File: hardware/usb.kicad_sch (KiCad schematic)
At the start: 35 parts, among them J1 USB_A_Stacked, J2 USB_C_Receptacle_USB2.0_14P, J3 USB_C_Receptacle_USB2.0_14P, J4 USB_C_Receptacle_USB2.0_14P, U10 SY6280AAC, U11 SY6280AAC, U12 SY6280AAC, U13 TPD2EUSB30, U14 TPD2EUSB30, U15 TPD2EUSB30, U16 TPD2EUSB30, U17 HUSB237, U18 TPD2EUSB30, U9 SY6280AAC

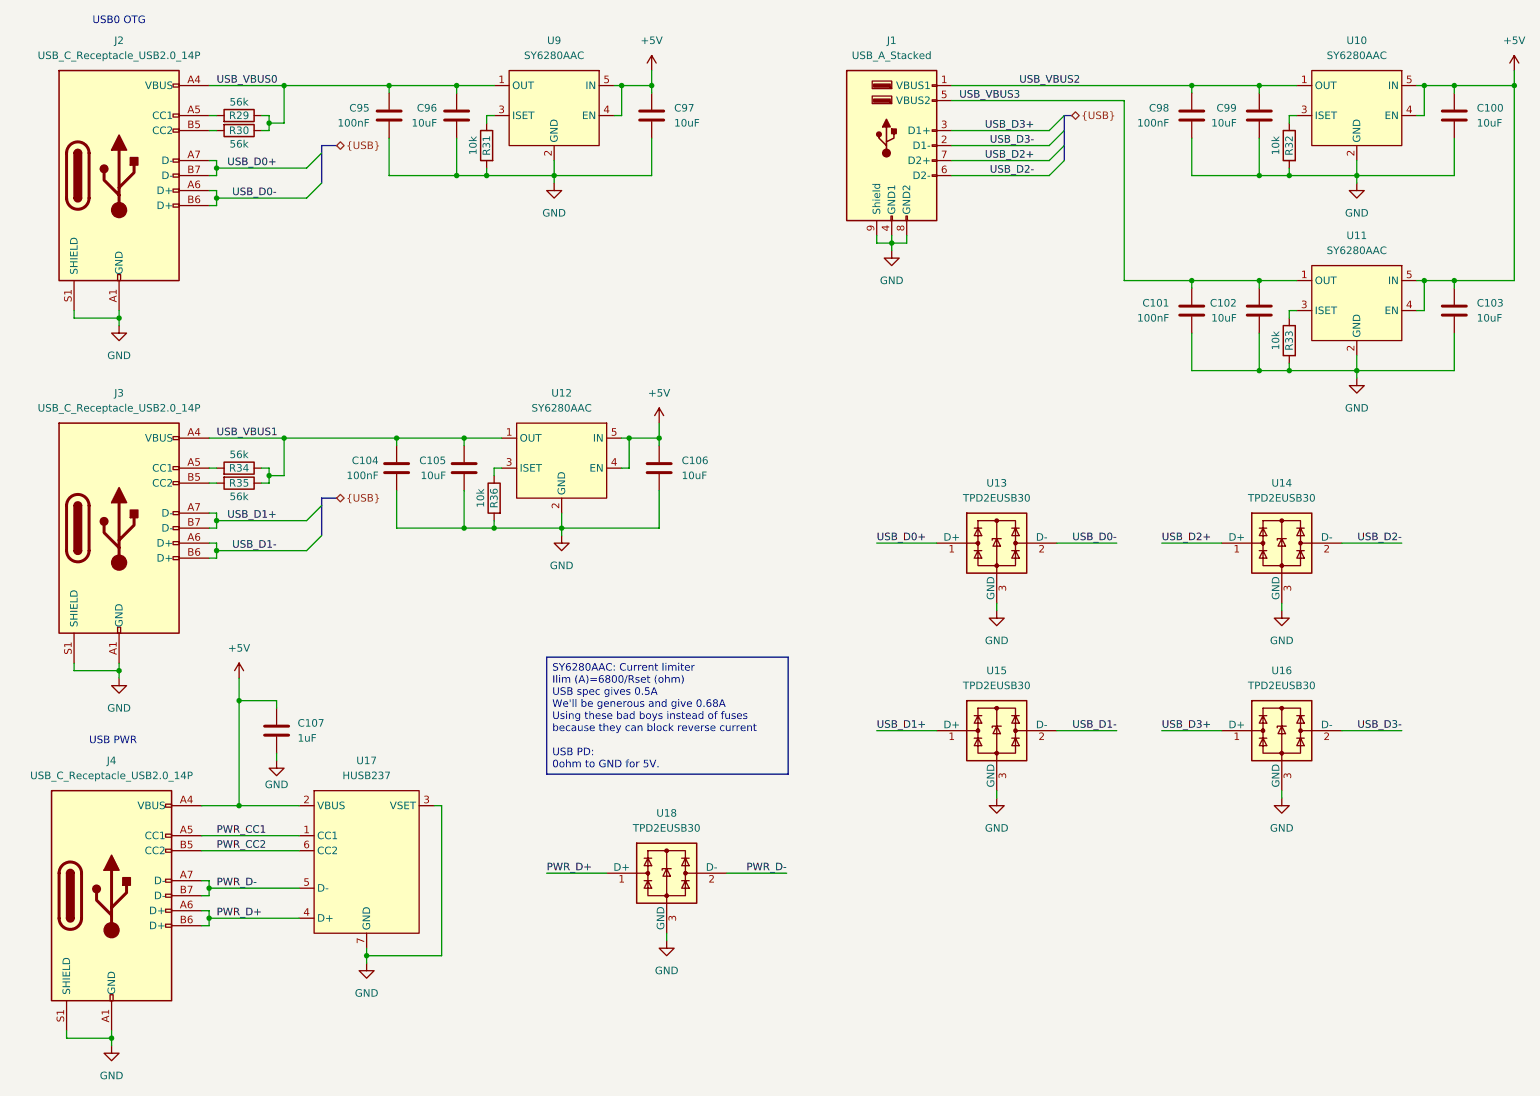
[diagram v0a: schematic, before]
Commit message: Improve heat dissipation and layout
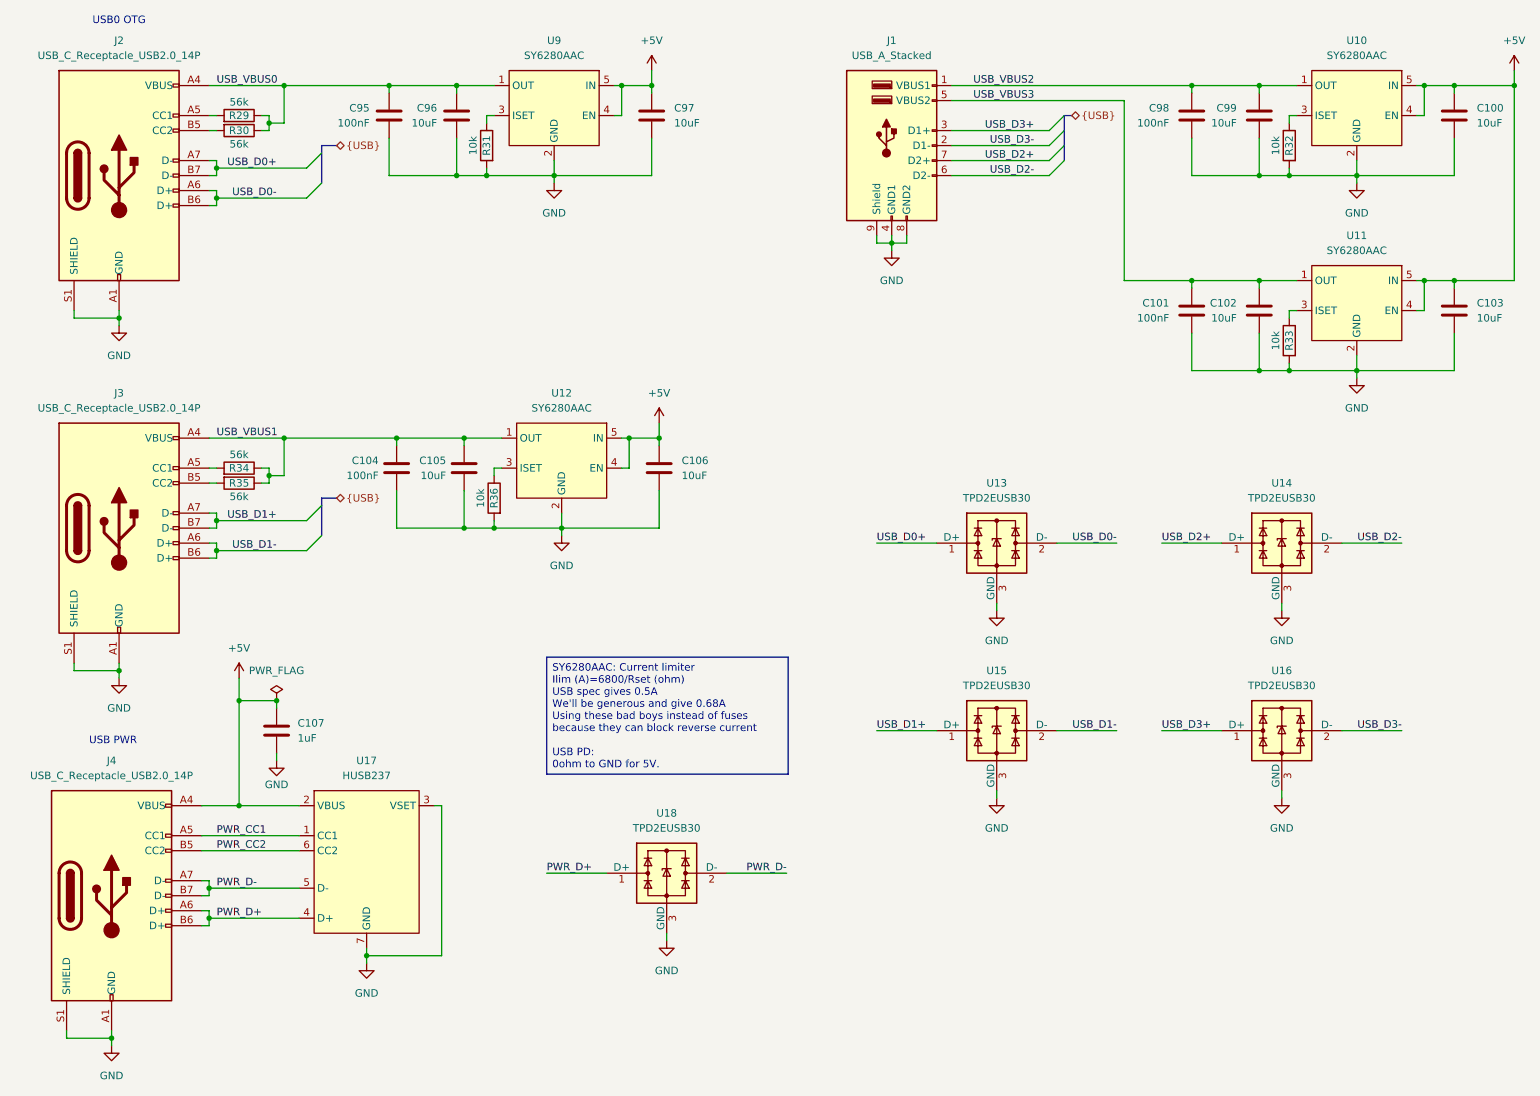
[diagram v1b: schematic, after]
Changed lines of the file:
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@@
 	)
 	(junction
+		(at 72.39 130.81)
+		(diameter 0)
+		(color 0 0 0 0)
+	)
+	(junction
 		(at 73.66 26.67)
 		(diameter 0)
@@
 	)
 	(label "USB_VBUS3"
-		(at 187.96 29.21 0)
+		(at 200.66 29.21 180)
 		(effects
 			(font
 				(size 1.27 1.27)
 			)
-			(justify left bottom)
+			(justify right bottom)
 		)
 	)
@@
 	)
 	(label "USB_VBUS2"
-		(at 198.12 26.67 0)
+		(at 200.66 26.67 180)
 		(effects
 			(font
 				(size 1.27 1.27)
 			)
-			(justify left bottom)
+			(justify right bottom)
 		)
 	)
@@
 	)
 	(symbol
+		(lib_id "power:PWR_FLAG")
+		(at 72.39 130.81 0)
+		(unit 1)
+		(exclude_from_sim no)
+		(in_bom yes)
+		(on_board yes)
+		(dnp no)
+		(fields_autoplaced yes)
+		(property "Reference" "#FLG07"
+			(at 72.39 128.905 0)
+			(effects
+				(font
+					(size 1.27 1.27)
+				)
+				(hide yes)
+			)
+		)
+		(property "Value" "PWR_FLAG"
+			(at 72.39 125.73 0)
+			(effects
+				(font
+					(size 1.27 1.27)
+				)
+			)
+		)
+		(property "Footprint" ""
+			(at 72.39 130.81 0)
+			(effects
+				(font
+					(size 1.27 1.27)
+				)
+				(hide yes)
+			)
+		)
+		(property "Datasheet" "~"
+			(at 72.39 130.81 0)
+			(effects
+				(font
+					(size 1.27 1.27)
+				)
+				(hide yes)
+			)
+		)
+		(property "Description" "Special symbol for telling ERC where power comes from"
+			(at 72.39 130.81 0)
+			(effects
+				(font
+					(size 1.27 1.27)
+				)
+				(hide yes)
+			)
+		)
+		(pin "1"
+		)
+		(instances
+			(project "cm0"
+				(path "/b53f5dbb-8078-4818-9e8f-fdf90ba6d854/62512c11-db29-412e-825e-173059bf3d51"
+					(reference "#FLG07")
+					(unit 1)
+				)
+			)
+		)
+	)
+	(symbol
 		(lib_id "Device:R")
 		(at 109.22 96.52 0)
@@
 	)
 	(symbol
+		(lib_name "SY6280AAC_1")
 		(lib_id "cm0:SY6280AAC")
 		(at 119.38 30.48 0)
@@
 	)
 	(symbol
+		(lib_name "SY6280AAC_2")
 		(lib_id "cm0:SY6280AAC")
 		(at 120.65 90.17 0)
@@
 	)
 	(symbol
+		(lib_name "SY6280AAC_3")
 		(lib_id "cm0:SY6280AAC")
 		(at 255.27 63.5 0)

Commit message: Add some more decoupling and move trace
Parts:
- J2, J3, J4: FT Position Offset 0,12.7 -> 0,2.81
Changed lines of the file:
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@@
 			)
 		)
-		(property "FT Position Offset" "0,12.7"
+		(property "FT Position Offset" "0,2.81"
 			(at 45.72 101.6 0)
 			(effects
@@
 			)
 		)
-		(property "FT Position Offset" "0,12.7"
+		(property "FT Position Offset" "0,2.81"
 			(at 45.72 41.91 0)
 			(effects
@@
 			)
 		)
-		(property "FT Position Offset" "0,12.7"
+		(property "FT Position Offset" "0,2.81"
 			(at 44.45 163.83 0)
 			(effects
